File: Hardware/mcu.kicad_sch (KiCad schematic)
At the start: 40 parts, among them J101 DEBUG, SW101 Button_Left, SW102 Button_Middle, SW103 Button_Right, SW104 Boot_Select, SW105 RESET, U101 RP2040, U102 W25Q128JVPIQ TR, X101 12MHz

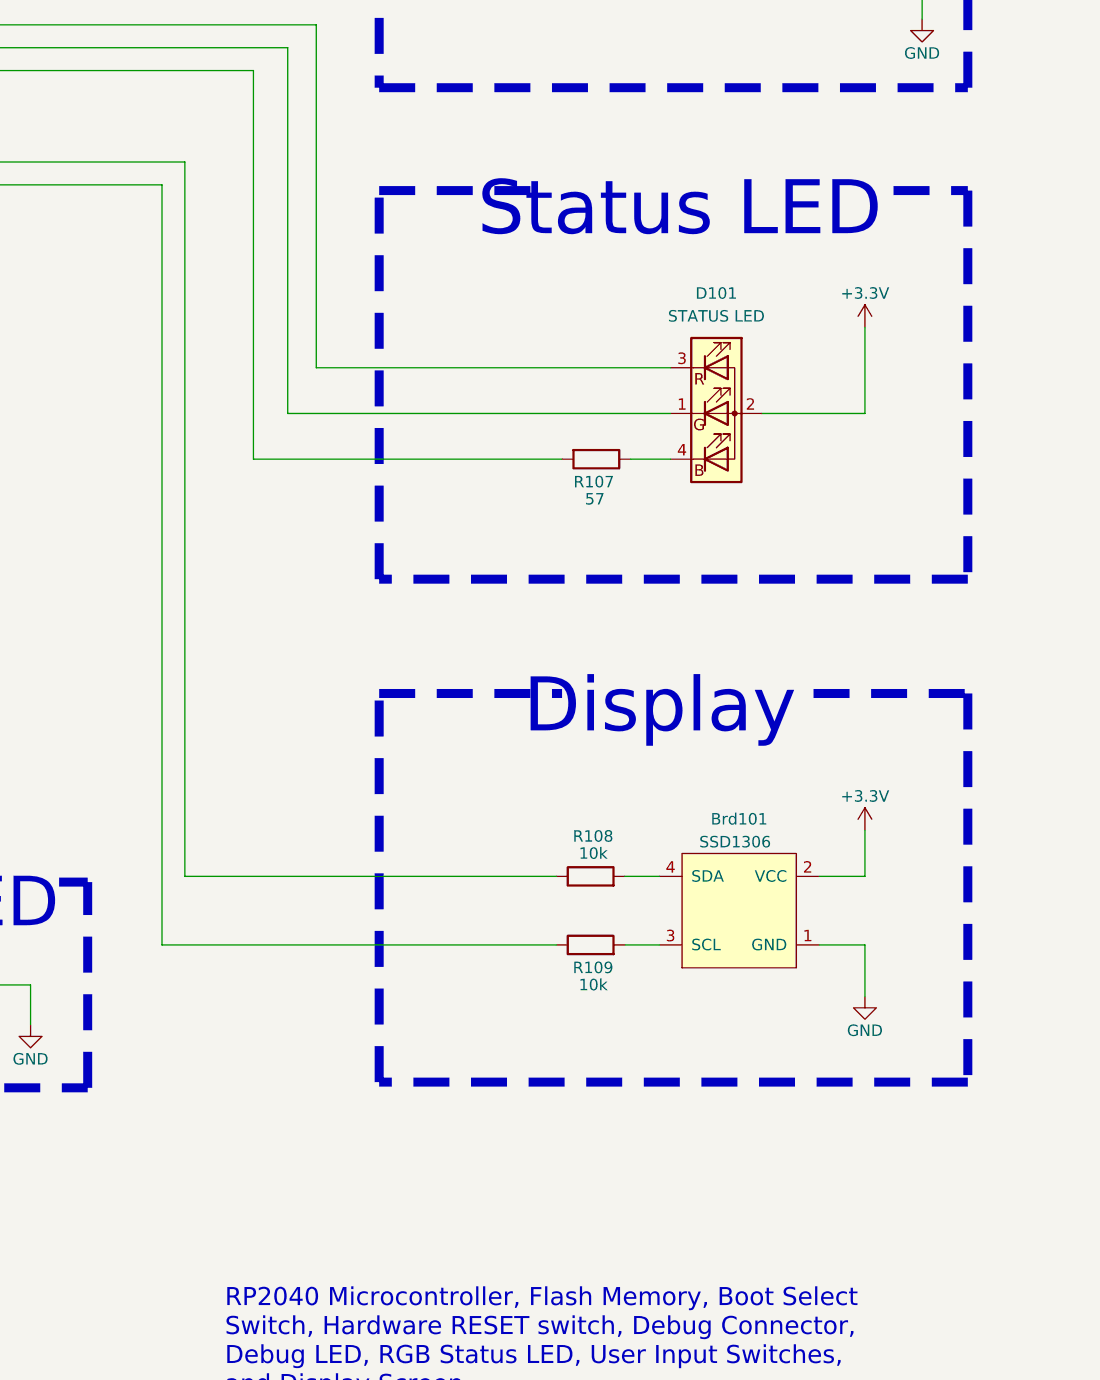
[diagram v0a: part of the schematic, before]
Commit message: Schematic update.
Changed I2C 10k resistors from series to pull-up.
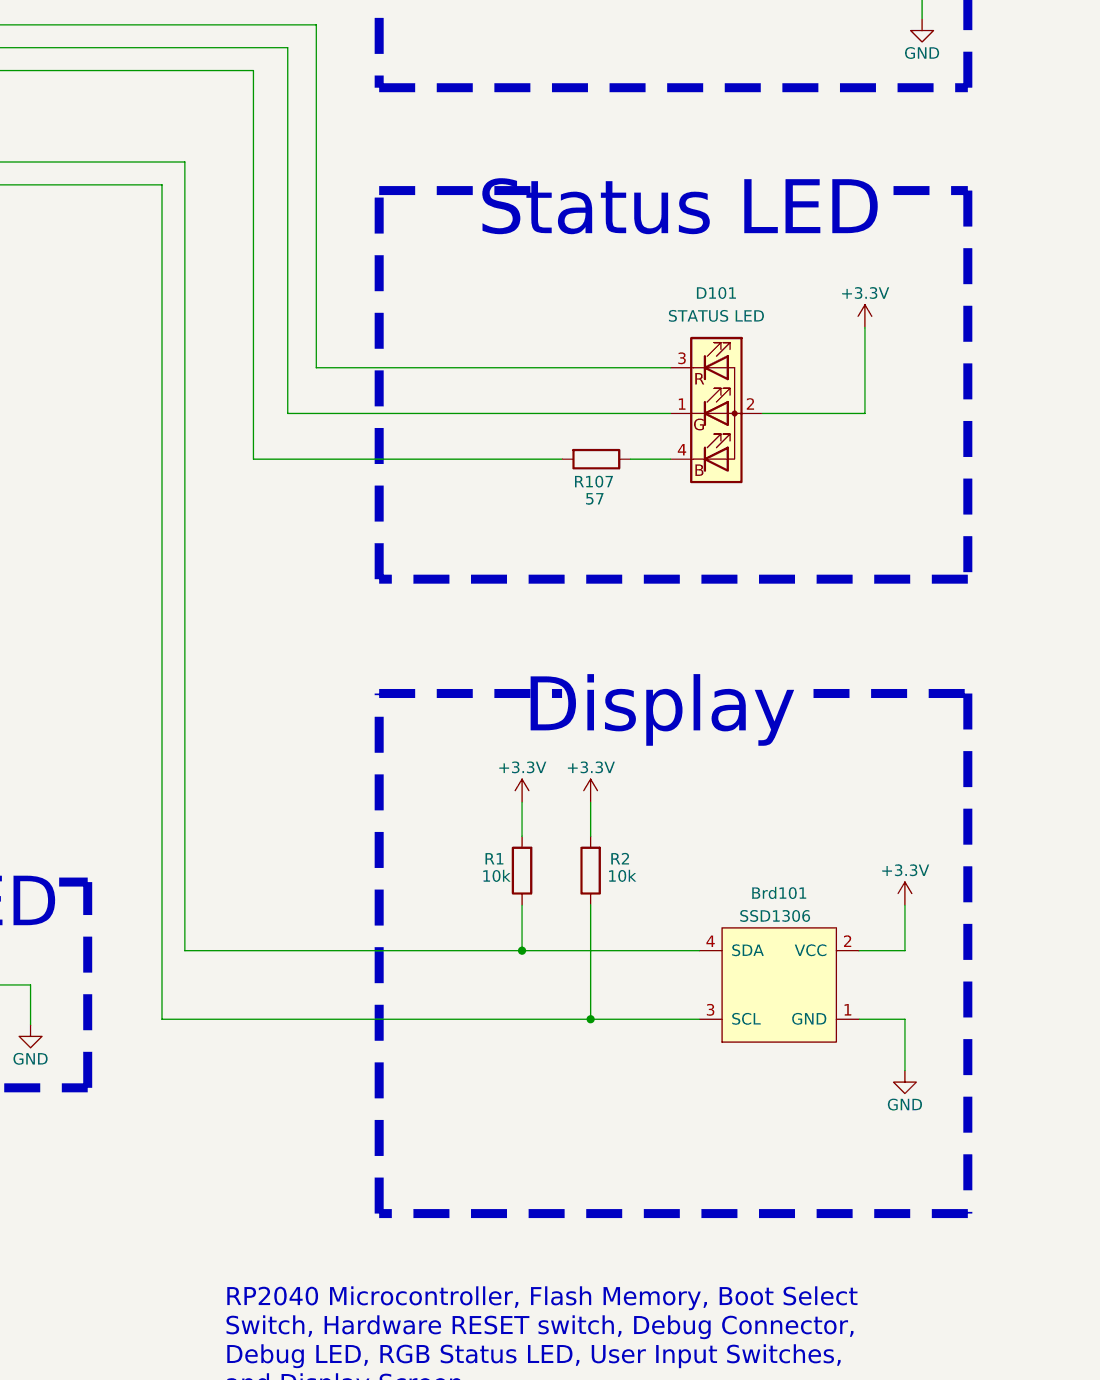
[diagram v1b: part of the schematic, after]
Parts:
- removed R108, R109: 10k, Resistor_SMD:R_0402_1005Metric, symbol RamaPotchi:R
- added R1, R2: 10k, Resistor_SMD:R_0402_1005Metric, symbol RamaPotchi:R
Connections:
- net +3.3V: now also R1.2, R2.2
- net I2C_SCL: now also Brd101.3 (SCL), R2.1
- net I2C_SDA: now also Brd101.4 (SDA), R1.1
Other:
- moved on the sheet: Brd101

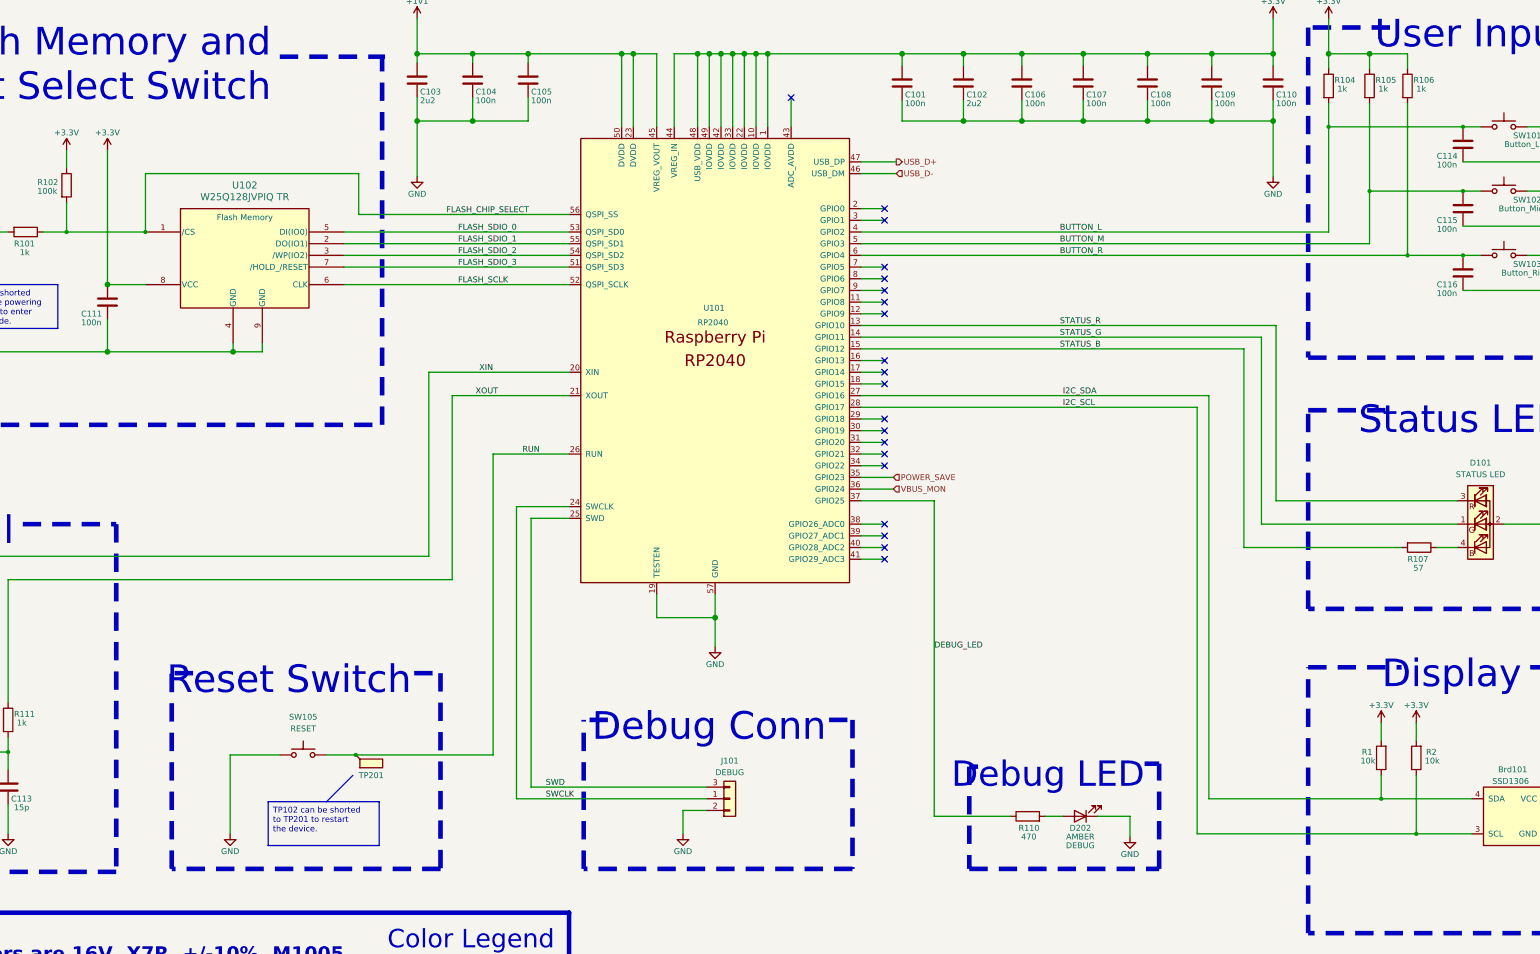
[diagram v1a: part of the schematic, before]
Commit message: Corrections
Added a pull-up resistor to run.
Adjusted resistance values of resistors on switches.
Add resistors to 2 LED legs.
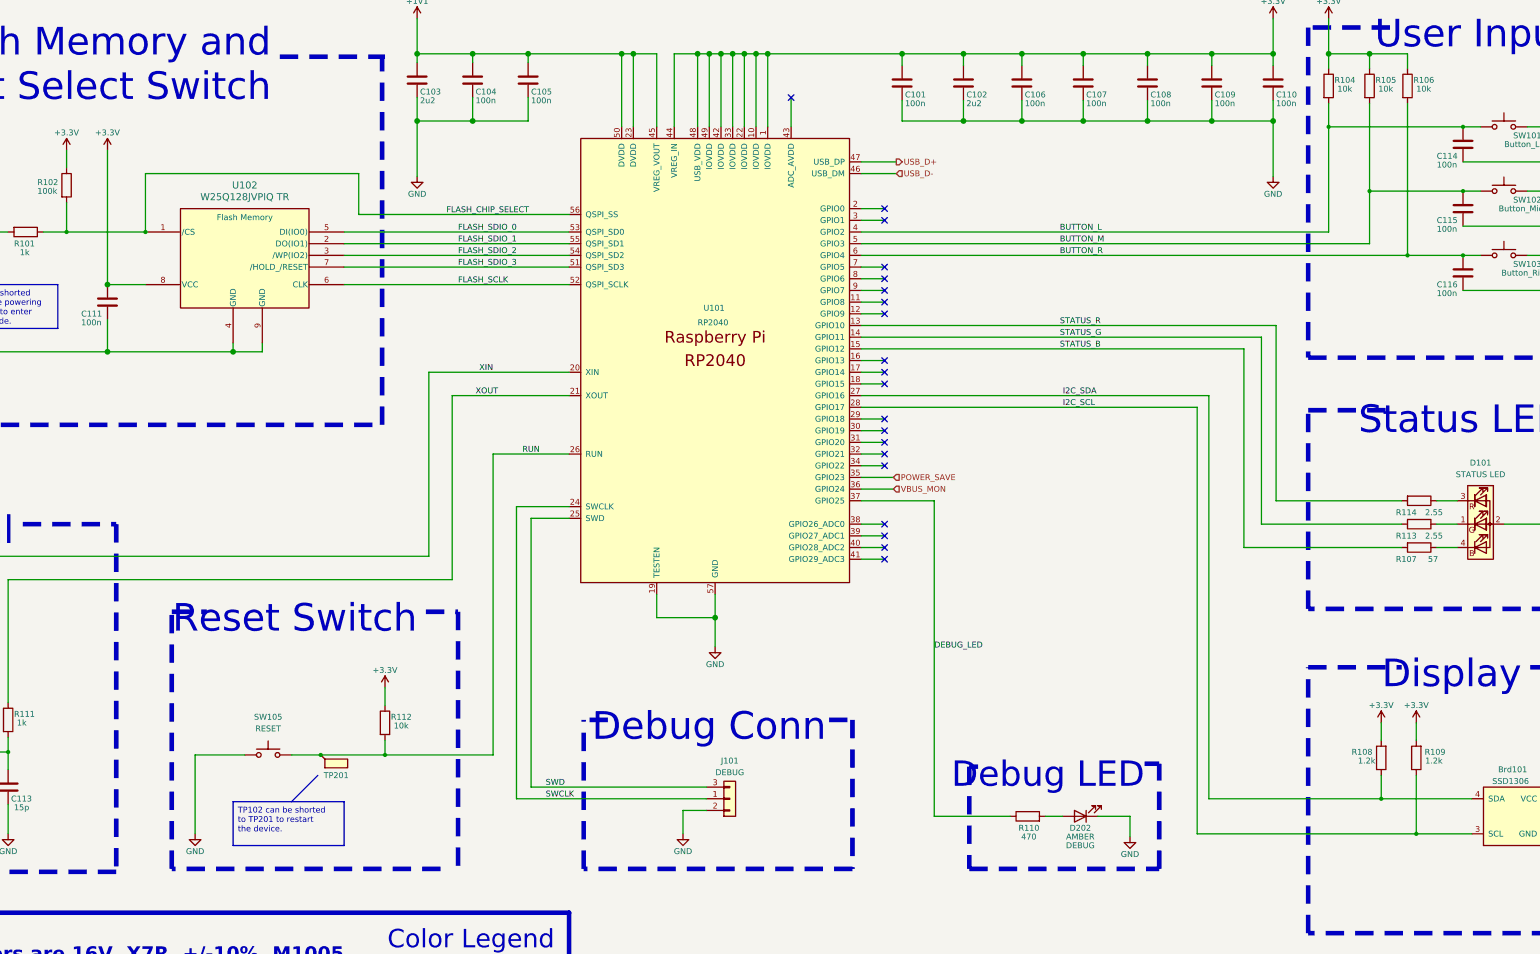
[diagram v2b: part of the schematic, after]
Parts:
- added R112: 10k, Resistor_SMD:R_0402_1005Metric, symbol RamaPotchi:R
- added R113, R114: 2.55, Resistor_SMD:R_0402_1005Metric, symbol RamaPotchi:R
- R104, R105, R106: value 1k -> 10k
- R108: renamed from R1; value 10k -> 1.2k
- R109: renamed from R2; value 10k -> 1.2k
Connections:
- net +3.3V: now also R112.1
- net RUN: now also R112.2
- net STATUS_G: now also R113.2; no longer D101.1 (GK)
- net STATUS_R: now also R114.2; no longer D101.3 (RK)
- new net: D101.1 (GK), R113.1
- new net: D101.3 (RK), R114.1
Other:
- moved on the sheet: SW105, TP201

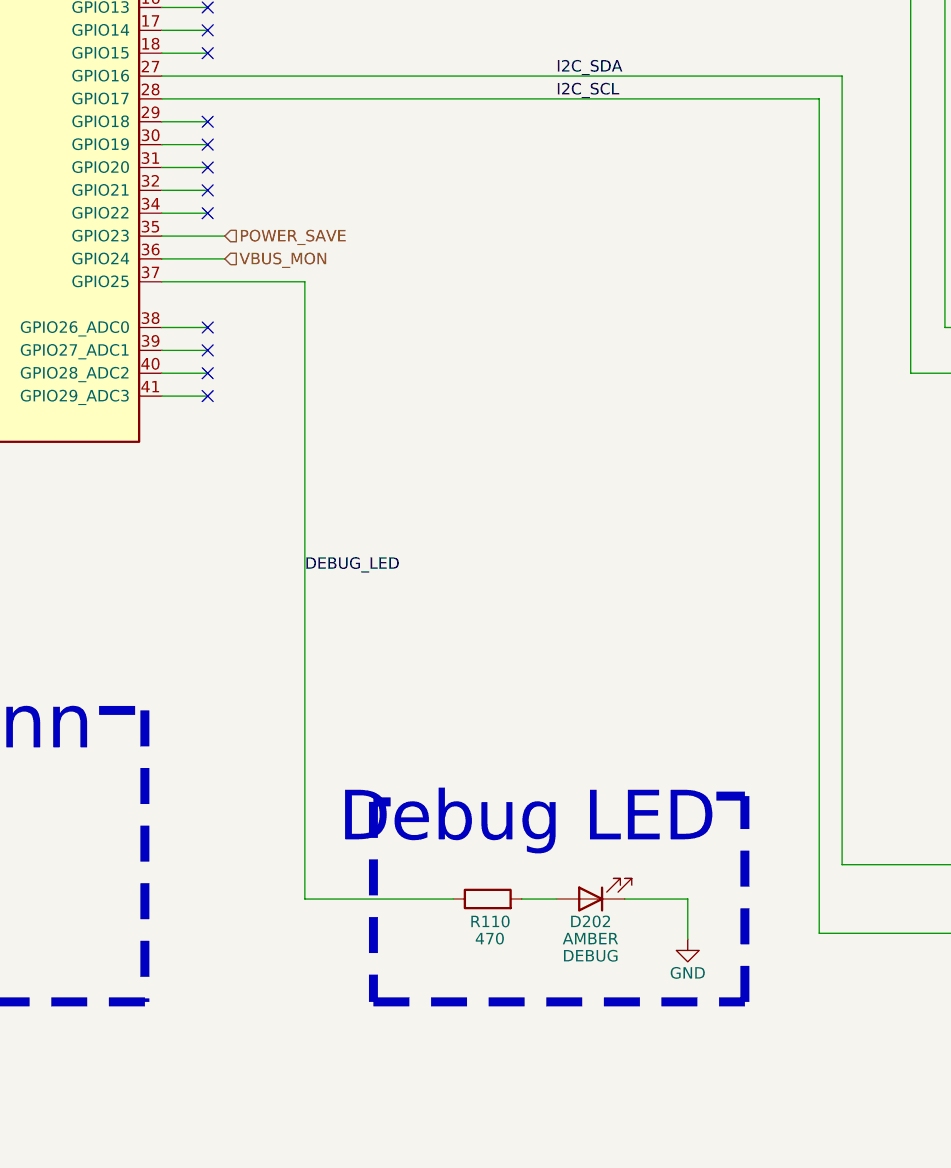
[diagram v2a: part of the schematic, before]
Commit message: Add Speaker
Added a passive tone buzzer to the schematic, to allow audible feedback.
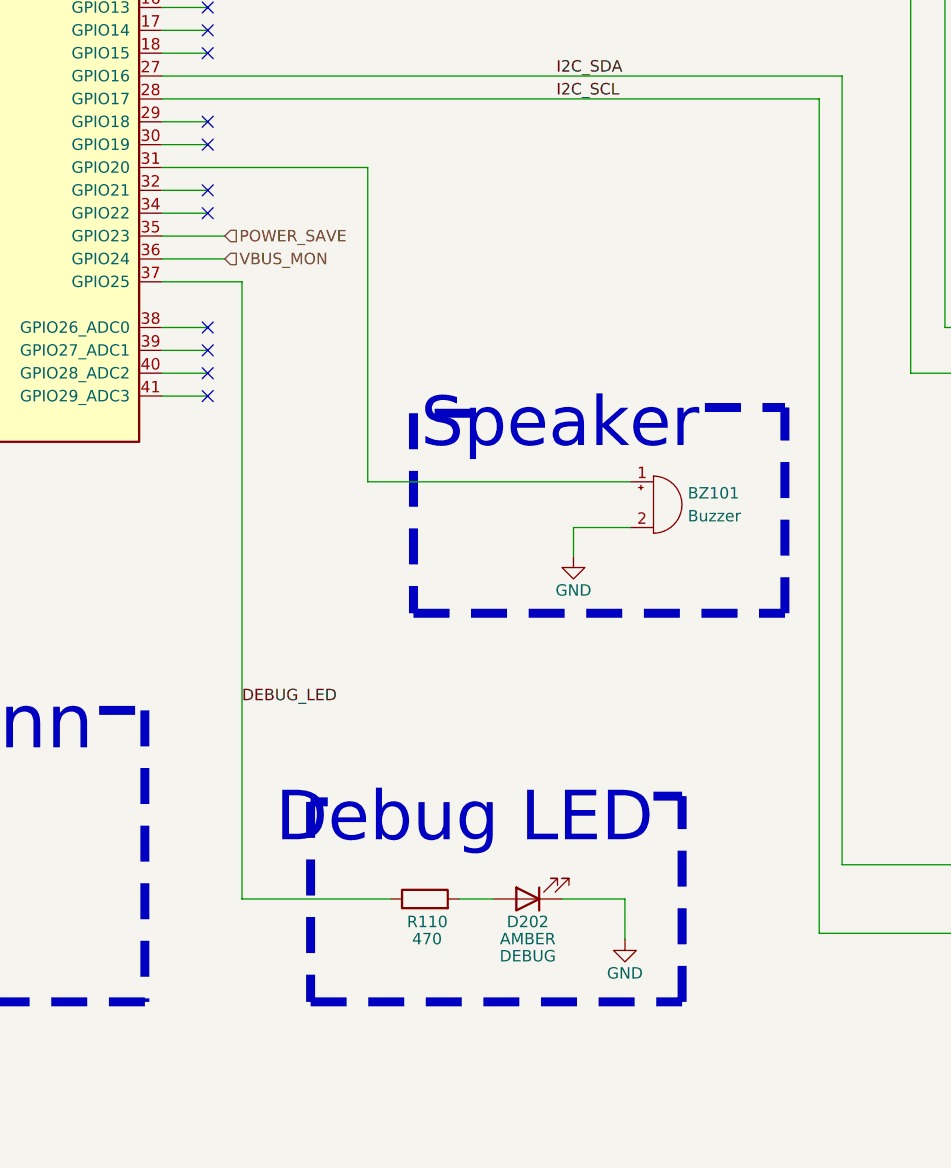
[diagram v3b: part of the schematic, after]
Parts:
- added BZ101: Buzzer, symbol Device:Buzzer
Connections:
- net GND: now also BZ101.2 (+)
- net at U101.31 (GPIO20): now also BZ101.1 (-)
- no-connect marks 26 -> 25
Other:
- note added: "Speaker"
- moved on the sheet: D202, R110

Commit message: Updated Description
Updated the text description on the schematic to include the speaker.
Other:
- note added: "RP2040 Microcontroller, Flash Memory, Boot Select Switch, Hardware RESET switch, Debug Connector, Debug LED, RGB Status LED, User Input Switches, Speaker, and Display Screen."
- note removed: "RP2040 Microcontroller, Flash Memory, Boot Select Switch, Hardware RESET switch, Debug Connector, Debug LED, RGB Status LED, User Input Switches, and Display Screen."
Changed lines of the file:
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@@
     (effects (font (face "Gill Sans MT") (size 6 6) (color 132 0 0 1)) (justify right bottom))
   )
-  (text "RP2040 Microcontroller, Flash Memory, Boot Select \nSwitch, Hardware RESET switch, Debug Connector,\nDebug LED, RGB Status LED, User Input Switches, \nand Display Screen."
+  (text "RP2040 Microcontroller, Flash Memory, Boot Select \nSwitch, Hardware RESET switch, Debug Connector,\nDebug LED, RGB Status LED, User Input Switches, \nSpeaker, and Display Screen."
     (at 323.85 267.335 0)
     (effects (font (size 2 2)) (justify left bottom))

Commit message: Update Battery Footprint
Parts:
- X101: footprint (none) -> Crystal:Crystal_SMD_0603-4Pin_6.0x3.5mm
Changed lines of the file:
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@@
       (effects (font (size 1.27 1.27)))
     )
-    (property "Footprint" "" (at 48.26 207.645 0)
+    (property "Footprint" "Crystal:Crystal_SMD_0603-4Pin_6.0x3.5mm" (at 48.26 207.645 0)
       (effects (font (size 1.27 1.27)) hide)
     )
-    (property "Datasheet" "~" (at 48.26 207.645 0)
+    (property "Datasheet" "https://ecsxtal.com/store/pdf/ecx_64r.pdf" (at 48.26 207.645 0)
       (effects (font (size 1.27 1.27)) hide)
     )
